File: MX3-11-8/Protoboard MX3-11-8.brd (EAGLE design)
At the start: 74 x 99.4 mm, 719 parts, among them J1 DCJ0202

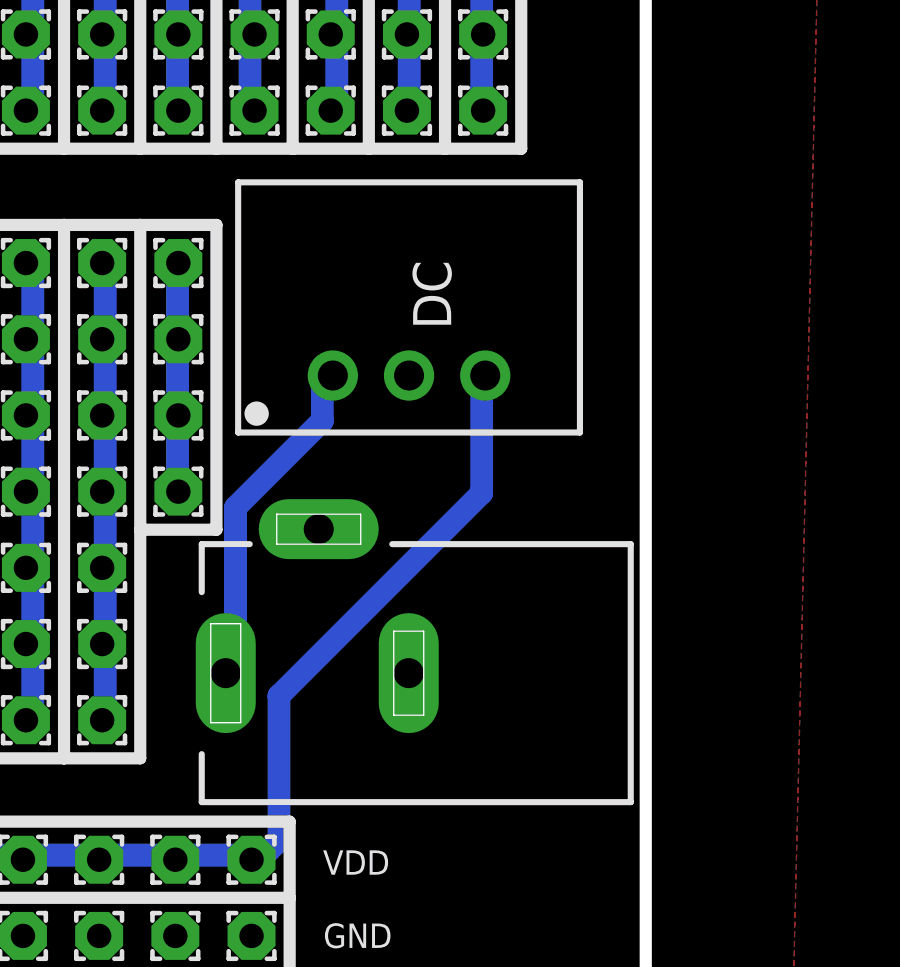
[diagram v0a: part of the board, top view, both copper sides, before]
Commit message: Update Gerb files
Created Gerber files for MX 2-7-6 without ESP
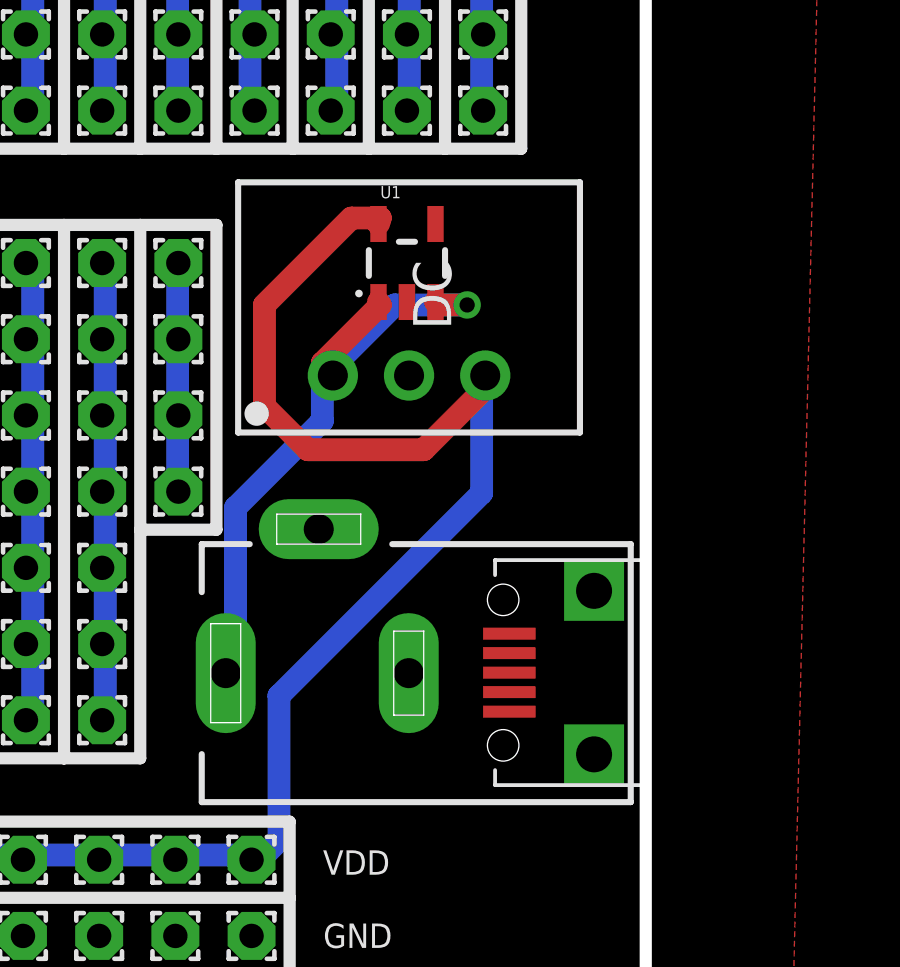
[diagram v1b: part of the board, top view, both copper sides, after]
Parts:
- added JP1: USB-RECEPTABLE, daspilker:FCI-10103594-0001LF
- added U1: 3.3V/150mA, SparkFun-PowerIC:SOT23-5
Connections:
- net GND: now also JP1.5, U1.2
- net VCC: now also JP1.1, U1.1, U1.3
- net VDD: now also U1.5
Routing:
- net VDD: track 226.3 -> 244.6 mm
- net VCC: track 11.6 -> 21.7 mm, vias 0 -> 1
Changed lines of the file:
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@@
 <?xml version="1.0" encoding="utf-8"?>
 <!DOCTYPE eagle SYSTEM "eagle.dtd">
-<eagle version="7.6.0">
+<eagle version="7.7.0">
 <drawing>
 <settings>
@@
 <setting verticaltext="up"/>
 </settings>
-<grid distance="1.27" unitdist="mm" unit="mm" style="dots" multiple="1" display="yes" altdistance="0.1" altunitdist="mm" altunit="mm"/>
+<grid distance="1.27" unitdist="mm" unit="mil" style="dots" multiple="1" display="yes" altdistance="12.5" altunitdist="mil" altunit="mil"/>
 <layers>
 <layer number="1" name="Top" color="4" fill="1" visible="yes" active="yes"/>
@@
 <autorouter>
 <pass name="Default">
-<param name="RoutingGrid" value="0.25mm"/>
+<param name="RoutingGrid" value="9.84251969mil"/>
 <param name="AutoGrid" value="1"/>
-<param name="Efforts" value="0"/>
+<param name="Efforts" value="1"/>
 <param name="TopRouterVariant" value="1"/>
 <param name="tpViaShape" value="round"/>
@@
 <attribute name="VALUE" x="25.4" y="74.26" size="0.0254" layer="27"/>
 </element>
+<element name="U1" library="SparkFun-PowerIC" package="SOT23-5" value="3.3V/150mA" x="66.04" y="27.94">
+<attribute name="PROD_ID" value="VREG-00822" x="66.04" y="27.94" size="1.778" layer="27" display="off"/>
+</element>
+<element name="JP1" library="daspilker" package="FCI-10103594-0001LF" value="USB-RECEPTABLE" x="73.9775" y="14.2875" smashed="yes" rot="R90"/>
 </elements>
 <signals>
@@
 <contactref element="PAD339" pad="1"/>
 <contactref element="PAD331" pad="1"/>
+<contactref element="JP1" pad="5"/>
+<contactref element="U1" pad="2"/>
 </signal>
 <signal name="VCC">
@@
 <wire x1="63.2206" y1="24.13" x2="63.57" y2="24.19" width="0.762" layer="16"/>
 <wire x1="60.325" y1="14.478" x2="60" y2="14.27" width="0.762" layer="16"/>
+<contactref element="JP1" pad="1"/>
+<contactref element="U1" pad="3"/>
+<contactref element="U1" pad="1"/>
+<wire x1="63.2206" y1="24.6126" x2="65.151" y2="26.543" width="0.762" layer="1"/>
+<wire x1="65.151" y1="26.543" x2="65.09" y2="26.6399" width="0.762" layer="1"/>
+<wire x1="63.2206" y1="24.6126" x2="63.57" y2="24.19" width="0.762" layer="1"/>
+<wire x1="68.0466" y1="26.543" x2="67.0814" y2="26.543" width="0.762" layer="1"/>
+<wire x1="65.6336" y1="26.543" x2="68.0466" y2="26.543" width="0.762" layer="16"/>
+<wire x1="63.7032" y1="24.6126" x2="65.6336" y2="26.543" width="0.762" layer="16"/>
+<wire x1="67.0814" y1="26.543" x2="66.99" y2="26.6399" width="0.762" layer="1"/>
+<wire x1="63.7032" y1="24.6126" x2="63.57" y2="24.19" width="0.762" layer="16"/>
+<via x="68.0466" y="26.543" extent="1-16" drill="0.508"/>
+<wire x1="60.325" y1="14.478" x2="69.4525" y2="12.9875" width="0" layer="19" extent="1-16"/>
 </signal>
 <signal name="N$1">
@@
 <wire x1="4.826" y1="91.2114" x2="5.08" y2="91.44" width="0.762" layer="16"/>
 <wire x1="4.826" y1="8.2042" x2="4.98" y2="8.05" width="0.762" layer="16"/>
+<contactref element="U1" pad="5"/>
+<wire x1="64.1858" y1="29.4386" x2="65.151" y2="29.4386" width="0.762" layer="1"/>
+<wire x1="61.2902" y1="26.543" x2="64.1858" y2="29.4386" width="0.762" layer="1"/>
+<wire x1="61.2902" y1="23.1648" x2="61.2902" y2="26.543" width="0.762" layer="1"/>
+<wire x1="62.738" y1="21.717" x2="61.2902" y2="23.1648" width="0.762" layer="1"/>
+<wire x1="66.5988" y1="21.717" x2="62.738" y2="21.717" width="0.762" layer="1"/>
+<wire x1="69.0118" y1="24.13" x2="66.5988" y2="21.717" width="0.762" layer="1"/>
+<wire x1="65.151" y1="29.4386" x2="65.09" y2="29.2401" width="0.762" layer="1"/>
+<wire x1="69.0118" y1="24.13" x2="68.65" y2="24.19" width="0.762" layer="1"/>
 </signal>
 <signal name="N$3">

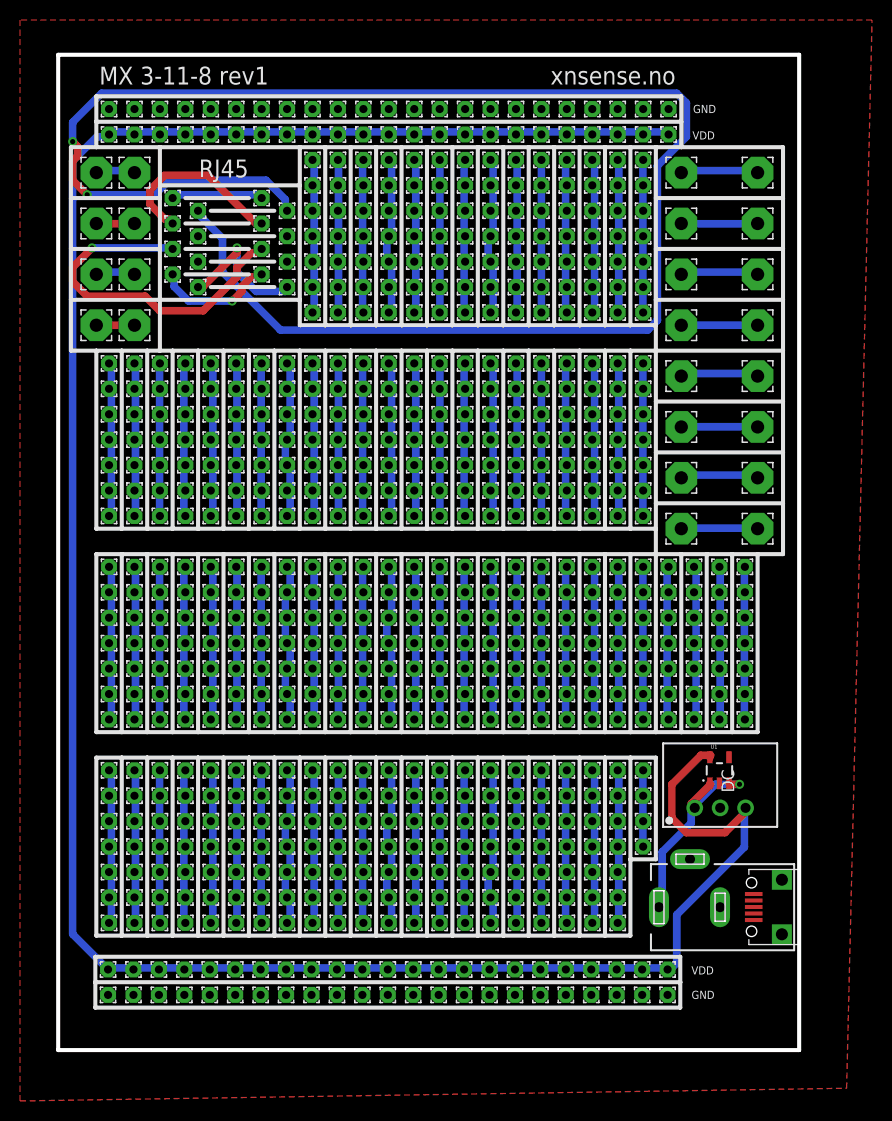
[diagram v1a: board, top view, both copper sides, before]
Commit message: Update to rev2
Updated to Pin headers instead of single wire pads
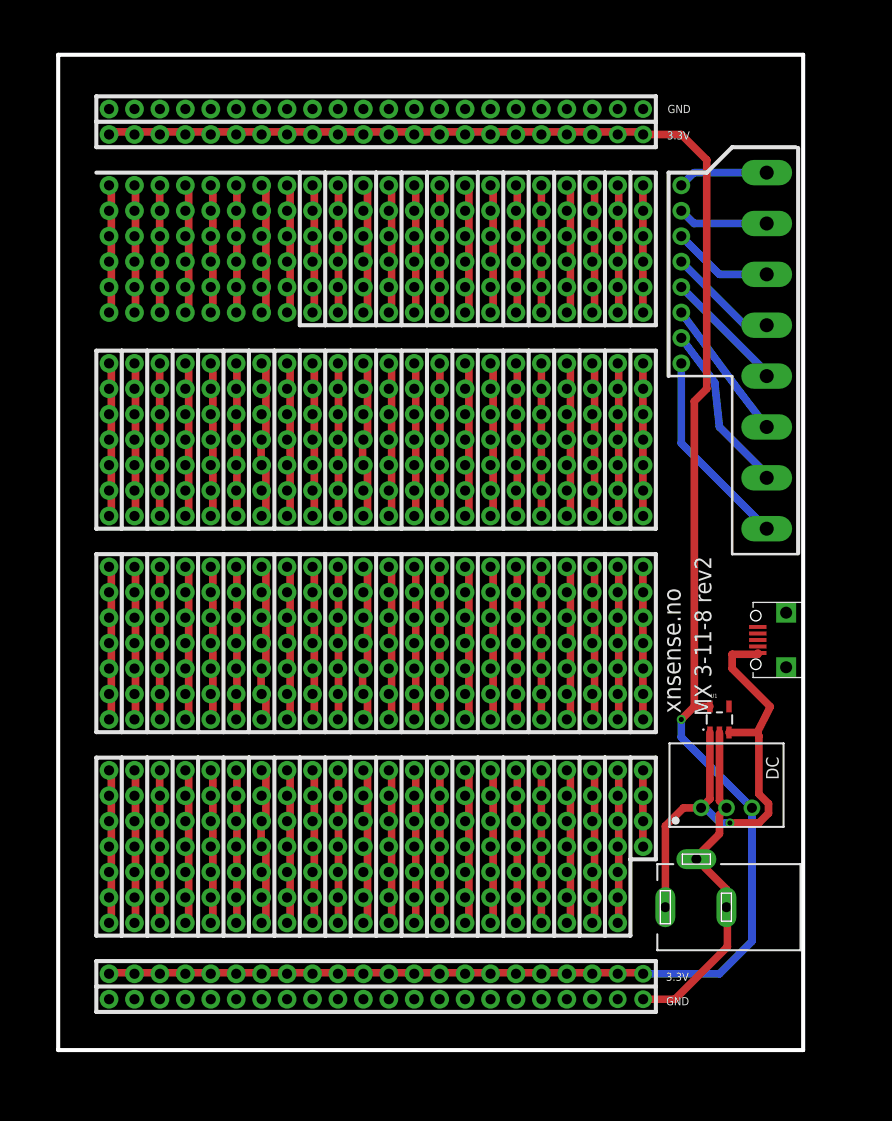
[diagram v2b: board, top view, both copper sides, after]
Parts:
- removed 1, 2, 3, 4, 5, 6, 7, 8, PAD1, PAD10, PAD100, PAD101, PAD102, PAD103, PAD104, PAD105, PAD106, PAD107, PAD108, PAD109, PAD11, PAD110, PAD111, PAD112, PAD113, PAD114, PAD115, PAD116, PAD117, PAD118, PAD119, PAD12, PAD120, PAD121, PAD122, PAD123, PAD124, PAD125, PAD126, PAD127, PAD128, PAD129, PAD13, PAD130, PAD131, PAD132, PAD133, PAD134, PAD135, PAD136, PAD137, PAD138, PAD139, PAD14, PAD140, PAD141, PAD142, PAD143, PAD144, PAD145, PAD146, PAD147, PAD148, PAD149, PAD15, PAD150, PAD151, PAD152, PAD153, PAD154, PAD155, PAD156, PAD157, PAD158, PAD159, PAD16, PAD160, PAD161, PAD162, PAD163, PAD164, PAD165, PAD166, PAD167, PAD168, PAD169, PAD17, PAD170, PAD171, PAD172, PAD173, PAD174, PAD175, PAD176, PAD177, PAD178, PAD179, PAD18, PAD180, PAD181, PAD182, PAD183, PAD184, PAD185, PAD186, PAD187, PAD188, PAD189, PAD19, PAD190, PAD191, PAD192, PAD193, PAD194, PAD195, PAD196, PAD197, PAD198, PAD199, PAD2, PAD20, PAD200, PAD201, PAD202, PAD203, PAD204, PAD205, PAD206, PAD207, PAD208, PAD209, PAD21, PAD210, PAD211, PAD212, PAD213, PAD214, PAD215, PAD216, PAD217, PAD218, PAD219, PAD22, PAD220, PAD221, PAD222, PAD223, PAD224, PAD225, PAD226, PAD227, PAD228, PAD229, PAD23, PAD230, PAD231, PAD232, PAD233, PAD234, PAD235, PAD236, PAD237, PAD238, PAD239, PAD24, PAD240, PAD249, PAD25, PAD250, PAD251, PAD252, PAD253, PAD254, PAD255, PAD26, PAD260, PAD261, PAD262, PAD263, PAD264, PAD265, PAD266, PAD269, PAD27, PAD270, PAD271, PAD272, PAD273, PAD274, PAD275, PAD276, PAD277, PAD278, PAD279, PAD28, PAD280, PAD281, PAD282, PAD283, PAD284, PAD285, PAD286, PAD287, PAD288, PAD289, PAD29, PAD290, PAD291, PAD292, PAD293, PAD294, PAD295, PAD296, PAD297, PAD298, PAD299, PAD3, PAD30, PAD300, PAD301, PAD302, PAD303, PAD304, PAD305, PAD306, PAD307, PAD308, PAD309, PAD31, PAD310, PAD311, PAD312, PAD313, PAD314, PAD315, PAD316, PAD317, PAD318, PAD319, PAD32, PAD320, PAD321, PAD322, PAD323, PAD324, PAD325, PAD326, PAD327, PAD328, PAD329, PAD33, PAD330, PAD331, PAD332, PAD333, PAD334, PAD335, PAD336, PAD337, PAD338, PAD339, PAD34, PAD340, PAD341, PAD342, PAD343, PAD344, PAD345, PAD346, PAD347, PAD348, PAD349, PAD35, PAD350, PAD351, PAD352, PAD353, PAD354, PAD355, PAD356, PAD357, PAD358, PAD359, PAD36, PAD360, PAD361, PAD362, PAD363, PAD364, PAD365, PAD366, PAD367, PAD368, PAD369, PAD37, PAD370, PAD371, PAD372, PAD373, PAD374, PAD375, PAD376, PAD377, PAD378, PAD379, PAD38, PAD380, PAD381, PAD382, PAD383, PAD384, PAD385, PAD386, PAD387, PAD388, PAD389, PAD39, PAD390, PAD391, PAD392, PAD393, PAD394, PAD395, PAD4, PAD40, PAD41, PAD414, PAD415, PAD416, PAD42, PAD420, PAD421, PAD422, PAD423, PAD424, PAD425, PAD426, PAD427, PAD428, PAD429, PAD43, PAD430, PAD431, PAD432, PAD433, PAD434, PAD435, PAD436, PAD437, PAD438, PAD439, PAD44, PAD440, PAD441, PAD442, PAD443, PAD444, PAD445, PAD446, PAD447, PAD448, PAD449, PAD45, PAD450, PAD451, PAD452, PAD453, PAD454, PAD455, PAD456, PAD457, PAD458, PAD459, PAD46, PAD460, PAD461, PAD462, PAD463, PAD464, PAD465, PAD466, PAD467, PAD468, PAD469, PAD47, PAD470, PAD471, PAD472, PAD473, PAD474, PAD475, PAD476, PAD477, PAD478, PAD479, PAD48, PAD480, PAD481, PAD482, PAD483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: (no value), wirepad:1,6/0,8
- removed PAD241, PAD242, PAD243, PAD244, PAD245, PAD246, PAD247, PAD248, PAD734, PAD735, PAD736, PAD737, PAD738, PAD739, PAD740, PAD741, PAD750, PAD751, PAD752, PAD753, PAD754, PAD755, PAD756, PAD757: (no value), wirepad:3,17/1,3
- added J10, J11, J12, J13, J14, J15, J16, J17, J18, J19, J2, J20, J21, J22, J23, J3, J4, J5, J6, J7, J8, J9: (no value), SparkFun-Connectors:1X06_NO_SILK
- added J24, J25, J26, J27, J28, J29, J30, J31, J32, J33, J34, J35, J36, J37, J38, J39, J40, J41, J42, J43, J44, J45, J46, J47, J48, J49, J50, J51, J52, J53, J54, J55, J56, J57, J58, J59, J60, J61, J62, J63, J64, J65, J66, J67, J68, J69, J70, J71, J72, J73, J74, J75, J76, J77, J78, J79, J80, J81, J82, J83, J84, J85, J86, J87, J88: (no value), SparkFun-Connectors:1X07_NO_SILK
- added J89: (no value), SparkFun-Connectors:1X04_NO_SILK_ALL_ROUND
- added J90, J91, J92, J93: (no value), SparkFun-Connectors:1X20_NO_SILK_KIT
- added JP10, JP11, JP12, JP13, JP14, JP15, JP16, JP17, JP18, JP19, JP20, JP21, JP22, JP23, JP24, JP25: (no value), adafruit:1X01-CLEANBIG
- added JP2, JP3, JP4, JP5, JP6, JP7, JP8, JP9: (no value), adafruit:1X1-BIGPOGO
- moved JP1 26.7 mm to (74.4, 41.0)
- moved U1 5.08 mm to (66.0, 33.0)
- moved DC 0.64 mm to (66.7, 24.2)
- moved J1 0.63 mm to (63.7, 14.3)
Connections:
- removed net N$100: PAD699.1, PAD700.1, PAD701.1, PAD702.1, PAD703.1, PAD704.1, PAD705.1
- removed net N$101: PAD706.1, PAD707.1, PAD708.1, PAD709.1, PAD710.1, PAD711.1, PAD712.1
- removed net N$102: 1.1, RJ-1-1.1
- removed net N$103: 2.1, RJ-2-1.1
- removed net N$104: 3.1, RJ-3.1
- removed net N$105: 4.1, RJ-4-1.1
- removed net N$106: 5.1, RJ-5-1.1
- removed net N$107: 6.1, RJ-6-1.1
- removed net N$108: 7.1, RJ-7-1.1
- removed net N$109: 8.1, RJ-8-1.1
- removed net N$110: PAD713.1, PAD714.1, PAD715.1, PAD716.1, PAD717.1, PAD718.1, PAD719.1
- removed net N$111: PAD720.1, PAD721.1, PAD722.1, PAD723.1, PAD724.1, PAD725.1, PAD726.1
- removed net N$112: PAD727.1, PAD728.1, PAD729.1, PAD730.1, PAD731.1, PAD732.1, PAD733.1
- removed net N$113: PAD734.1, PAD757.1
- removed net N$114: PAD735.1, PAD756.1
- removed net N$115: PAD736.1, PAD755.1
- removed net N$116: PAD737.1, PAD754.1
- removed net N$117: PAD738.1, PAD753.1
- removed net N$118: PAD739.1, PAD752.1
- removed net N$119: PAD740.1, PAD751.1
- removed net N$120: PAD741.1, PAD750.1
- removed net N$97: PAD678.1, PAD679.1, PAD680.1, PAD681.1, PAD682.1, PAD683.1, PAD684.1
- removed net N$98: PAD685.1, PAD686.1, PAD687.1, PAD688.1, PAD689.1, PAD690.1, PAD691.1
- removed net N$99: PAD692.1, PAD693.1, PAD694.1, PAD695.1, PAD696.1, PAD697.1, PAD698.1
- new net N$47: J48.1, J48.2, J48.3, J48.4, J48.5, J48.6, J48.7
- new net N$48: J49.1, J49.2, J49.3, J49.4, J49.5, J49.6, J49.7
- new net N$52: J53.1, J53.2, J53.3, J53.4, J53.5, J53.6, J53.7
- new net N$53: J54.1, J54.2, J54.3, J54.4, J54.5, J54.6, J54.7
- new net N$54: J55.1, J55.2, J55.3, J55.4, J55.5, J55.6, J55.7
- new net N$55: J56.1, J56.2, J56.3, J56.4, J56.5, J56.6, J56.7
- new net N$56: J57.1, J57.2, J57.3, J57.4, J57.5, J57.6, J57.7
- new net N$57: J58.1, J58.2, J58.3, J58.4, J58.5, J58.6, J58.7
- new net N$58: J59.1, J59.2, J59.3, J59.4, J59.5, J59.6, J59.7
- new net N$85: J86.1, J86.2, J86.3, J86.4, J86.5, J86.6, J86.7
- new net N$86: J87.1, J87.2, J87.3, J87.4, J87.5, J87.6, J87.7
- new net N$87: J88.1, J88.2, J88.3, J88.4, J88.5, J88.6, J88.7
- new net N$88: J89.1, J89.2, J89.3, J89.4
- new net N$89: JP10.1, JP2.P$1
- new net N$90: JP11.1, JP3.P$1
- new net N$91: JP12.1, JP4.P$1
- net GND: now also J91.1, J91.10, J91.11, J91.12, J91.13, J91.14, J91.15, J91.16, J91.17, J91.18, J91.19, J91.2, J91.20, J91.3, J91.4, J91.5, J91.6, J91.7, J91.8, J91.9, J92.1, J92.10, J92.11, J92.12, J92.13, J92.14, J92.15, J92.16, J92.17, J92.18, J92.19, J92.2, J92.20, J92.3, J92.4, J92.5, J92.6, J92.7, J92.8, J92.9, JP20.1, JP21.1, JP23.1, JP24.1; no longer PAD17.1, PAD22.1, PAD23.1, PAD24.1, PAD25.1, PAD26.1, PAD27.1, PAD276.1, PAD277.1, PAD28.1, PAD285.1, PAD286.1, PAD29.1, PAD30.1, PAD31.1, PAD32.1, PAD326.1, PAD327.1, PAD328.1, PAD329.1, PAD33.1, PAD330.1, PAD331.1, PAD339.1, PAD36.1, PAD38.1, PAD4.1, PAD421.1, PAD422.1, PAD423.1, PAD424.1, PAD425.1, PAD426.1, PAD427.1, PAD428.1, PAD429.1, PAD430.1, PAD431.1, PAD432.1, PAD433.1, PAD434.1, PAD435.1, PAD436.1, PAD439.1, PAD440.1, PAD441.1
- net N$1: now also J2.1, J2.2, J2.3, J2.4, J2.5, J2.6; no longer PAD391.1, PAD392.1, PAD393.1, PAD394.1, PAD42.1, PAD43.1, PAD44.1
- net N$10: now also J11.1, J11.2, J11.3, J11.4, J11.5, J11.6; no longer PAD106.1, PAD107.1, PAD108.1, PAD109.1, PAD110.1, PAD111.1, PAD112.1
- net N$11: now also J12.1, J12.2, J12.3, J12.4, J12.5, J12.6; no longer PAD115.1, PAD116.1, PAD117.1, PAD118.1, PAD119.1, PAD120.1, PAD121.1
- net N$12: now also J13.1, J13.2, J13.3, J13.4, J13.5, J13.6; no longer PAD124.1, PAD125.1, PAD126.1, PAD127.1, PAD128.1, PAD129.1, PAD130.1
- net N$13: now also J14.1, J14.2, J14.3, J14.4, J14.5, J14.6; no longer PAD133.1, PAD134.1, PAD135.1, PAD136.1, PAD137.1, PAD138.1, PAD139.1
- net N$14: now also J15.1, J15.2, J15.3, J15.4, J15.5, J15.6; no longer PAD142.1, PAD143.1, PAD144.1, PAD145.1, PAD146.1, PAD147.1, PAD148.1
- net N$15: now also J16.1, J16.2, J16.3, J16.4, J16.5, J16.6; no longer PAD151.1, PAD152.1, PAD153.1, PAD154.1, PAD155.1, PAD156.1, PAD157.1
- net N$16: now also J17.1, J17.2, J17.3, J17.4, J17.5, J17.6; no longer PAD160.1, PAD161.1, PAD162.1, PAD163.1, PAD164.1, PAD165.1, PAD166.1
- net N$17: now also J18.1, J18.2, J18.3, J18.4, J18.5, J18.6; no longer PAD169.1, PAD170.1, PAD171.1, PAD172.1, PAD173.1, PAD174.1, PAD175.1
- net N$18: now also J19.1, J19.2, J19.3, J19.4, J19.5, J19.6; no longer PAD178.1, PAD179.1, PAD180.1, PAD181.1, PAD182.1, PAD183.1, PAD184.1
- net N$19: now also J20.1, J20.2, J20.3, J20.4, J20.5, J20.6; no longer PAD187.1, PAD188.1, PAD189.1, PAD190.1, PAD191.1, PAD192.1, PAD193.1
- net N$2: now also J3.1, J3.2, J3.3, J3.4, J3.5, J3.6; no longer PAD241.1, PAD248.1
- net N$20: now also J21.1, J21.2, J21.3, J21.4, J21.5, J21.6; no longer PAD196.1, PAD197.1, PAD198.1, PAD199.1, PAD200.1, PAD201.1, PAD202.1
- net N$21: now also J22.1, J22.2, J22.3, J22.4, J22.5, J22.6; no longer PAD205.1, PAD206.1, PAD207.1, PAD208.1, PAD209.1, PAD210.1, PAD211.1
- net N$22: now also J23.1, J23.2, J23.3, J23.4, J23.5, J23.6; no longer PAD214.1, PAD215.1, PAD216.1, PAD217.1, PAD218.1, PAD219.1, PAD220.1
- net N$23: now also J24.1, J24.2, J24.3, J24.4, J24.5, J24.6, J24.7; no longer PAD66.1, PAD67.1, PAD68.1, PAD69.1, PAD70.1, PAD71.1, PAD72.1
- net N$24: now also J25.1, J25.2, J25.3, J25.4, J25.5, J25.6, J25.7; no longer PAD73.1, PAD74.1, PAD75.1, PAD76.1, PAD77.1, PAD78.1, PAD86.1
- net N$25: now also J26.1, J26.2, J26.3, J26.4, J26.5, J26.6, J26.7; no longer PAD104.1, PAD105.1, PAD113.1, PAD114.1, PAD87.1, PAD95.1, PAD96.1
- net N$26: now also J27.1, J27.2, J27.3, J27.4, J27.5, J27.6, J27.7; no longer PAD122.1, PAD123.1, PAD131.1, PAD132.1
- net N$27: now also J28.1, J28.2, J28.3, J28.4, J28.5, J28.6, J28.7; no longer PAD260.1, PAD261.1, PAD262.1, PAD263.1, PAD264.1, PAD265.1, PAD266.1
- net N$28: now also J29.1, J29.2, J29.3, J29.4, J29.5, J29.6, J29.7; no longer PAD269.1, PAD270.1, PAD271.1, PAD272.1, PAD273.1, PAD274.1, PAD275.1
- net N$29: now also J30.1, J30.2, J30.3, J30.4, J30.5, J30.6, J30.7; no longer PAD278.1, PAD279.1, PAD280.1, PAD281.1, PAD282.1, PAD283.1, PAD284.1
- net N$3: now also J4.1, J4.2, J4.3, J4.4, J4.5, J4.6; no longer PAD1.1, PAD2.1, PAD3.1, PAD34.1, PAD35.1, PAD37.1, PAD40.1
- net N$30: now also J31.1, J31.2, J31.3, J31.4, J31.5, J31.6, J31.7; no longer PAD287.1, PAD288.1, PAD289.1, PAD290.1, PAD291.1, PAD292.1, PAD293.1
- net N$31: now also J32.1, J32.2, J32.3, J32.4, J32.5, J32.6, J32.7; no longer PAD296.1, PAD297.1, PAD298.1, PAD299.1, PAD300.1, PAD301.1, PAD302.1
- net N$32: now also J33.1, J33.2, J33.3, J33.4, J33.5, J33.6, J33.7; no longer PAD305.1, PAD306.1, PAD307.1, PAD308.1, PAD309.1, PAD310.1, PAD311.1
- net N$33: now also J34.1, J34.2, J34.3, J34.4, J34.5, J34.6, J34.7; no longer PAD314.1, PAD315.1, PAD316.1, PAD317.1, PAD318.1, PAD319.1, PAD320.1
- net N$34: now also J35.1, J35.2, J35.3, J35.4, J35.5, J35.6, J35.7; no longer PAD150.1, PAD158.1, PAD159.1, PAD167.1, PAD168.1, PAD176.1, PAD177.1
- net N$35: now also J36.1, J36.2, J36.3, J36.4, J36.5, J36.6, J36.7; no longer PAD332.1, PAD333.1, PAD334.1, PAD335.1, PAD336.1, PAD337.1, PAD338.1
- net N$36: now also J37.1, J37.2, J37.3, J37.4, J37.5, J37.6, J37.7; no longer PAD341.1, PAD342.1, PAD343.1, PAD344.1, PAD345.1, PAD346.1, PAD347.1
- net N$37: now also J38.1, J38.2, J38.3, J38.4, J38.5, J38.6, J38.7; no longer PAD350.1, PAD351.1, PAD352.1, PAD353.1, PAD354.1, PAD355.1, PAD356.1
- net N$38: now also J39.1, J39.2, J39.3, J39.4, J39.5, J39.6, J39.7; no longer PAD359.1, PAD360.1, PAD361.1, PAD362.1, PAD363.1, PAD364.1, PAD365.1
- net N$39: now also J40.1, J40.2, J40.3, J40.4, J40.5, J40.6, J40.7; no longer PAD368.1, PAD369.1, PAD370.1, PAD371.1, PAD372.1, PAD373.1, PAD374.1
- net N$4: now also J5.1, J5.2, J5.3, J5.4, J5.5, J5.6; no longer PAD45.1, PAD46.1, PAD47.1, PAD48.1, PAD49.1, PAD50.1, PAD51.1
- net N$40: now also J41.1, J41.2, J41.3, J41.4, J41.5, J41.6, J41.7; no longer PAD377.1, PAD378.1, PAD379.1, PAD380.1, PAD381.1, PAD382.1, PAD383.1
- net N$41: now also J42.1, J42.2, J42.3, J42.4, J42.5, J42.6, J42.7; no longer PAD385.1, PAD386.1, PAD387.1, PAD388.1, PAD389.1, PAD39.1, PAD41.1
- net N$42: now also J43.1, J43.2, J43.3, J43.4, J43.5, J43.6, J43.7; no longer PAD242.1, PAD247.1
- net N$43: now also J44.1, J44.2, J44.3, J44.4, J44.5, J44.6, J44.7; no longer PAD243.1, PAD246.1
- net N$44: now also J45.1, J45.2, J45.3, J45.4, J45.5, J45.6, J45.7; no longer PAD244.1, PAD245.1
- net N$45: now also J46.1, J46.2, J46.3, J46.4, J46.5, J46.6, J46.7; no longer PAD185.1, PAD186.1, PAD194.1, PAD195.1, PAD203.1, PAD204.1, PAD212.1
- net N$46: now also J47.1, J47.2, J47.3, J47.4, J47.5, J47.6, J47.7; no longer PAD249.1, PAD250.1, PAD251.1, PAD252.1, PAD253.1, PAD254.1, PAD255.1
- net N$49: now also J50.1, J50.2, J50.3, J50.4, J50.5, J50.6, J50.7; no longer PAD213.1, PAD221.1, PAD222.1, PAD223.1, PAD224.1, PAD225.1, PAD226.1
- net N$5: now also J6.1, J6.2, J6.3, J6.4, J6.5, J6.6; no longer PAD52.1, PAD53.1, PAD54.1, PAD55.1, PAD56.1, PAD57.1, PAD58.1
- net N$50: now also J51.1, J51.2, J51.3, J51.4, J51.5, J51.6, J51.7; no longer PAD227.1, PAD228.1, PAD229.1, PAD230.1, PAD231.1, PAD232.1, PAD233.1
- net N$51: now also J52.1, J52.2, J52.3, J52.4, J52.5, J52.6, J52.7; no longer PAD234.1, PAD235.1, PAD236.1, PAD237.1, PAD238.1, PAD239.1, PAD240.1
- net N$59: now also J60.1, J60.2, J60.3, J60.4, J60.5, J60.6, J60.7; no longer PAD340.1, PAD348.1, PAD349.1, PAD357.1, PAD358.1, PAD366.1, PAD367.1
- net N$6: now also J7.1, J7.2, J7.3, J7.4, J7.5, J7.6; no longer PAD59.1, PAD60.1, PAD61.1, PAD62.1, PAD63.1, PAD64.1, PAD65.1
- net N$60: now also J61.1, J61.2, J61.3, J61.4, J61.5, J61.6, J61.7; no longer PAD375.1, PAD376.1, PAD384.1, PAD390.1, PAD395.1, PAD414.1, PAD415.1
- net N$61: now also J62.1, J62.2, J62.3, J62.4, J62.5, J62.6, J62.7; no longer PAD416.1, PAD420.1, PAD437.1, PAD438.1, PAD457.1, PAD458.1, PAD463.1
- net N$62: now also J63.1, J63.2, J63.3, J63.4, J63.5, J63.6, J63.7; no longer PAD464.1, PAD465.1, PAD466.1, PAD467.1, PAD468.1, PAD469.1, PAD470.1
- net N$63: now also J64.1, J64.2, J64.3, J64.4, J64.5, J64.6, J64.7; no longer PAD140.1, PAD141.1, PAD149.1, PAD471.1, PAD472.1, PAD473.1, PAD474.1
- net N$64: now also J65.1, J65.2, J65.3, J65.4, J65.5, J65.6, J65.7; no longer PAD475.1, PAD476.1, PAD477.1, PAD478.1, PAD479.1, PAD480.1, PAD481.1
- net N$65: now also J66.1, J66.2, J66.3, J66.4, J66.5, J66.6, J66.7; no longer PAD482.1, PAD483.1, PAD484.1, PAD485.1, PAD486.1, PAD487.1, PAD488.1
- net N$66: now also J67.1, J67.2, J67.3, J67.4, J67.5, J67.6, J67.7; no longer PAD489.1, PAD490.1, PAD491.1, PAD492.1, PAD493.1, PAD494.1, PAD495.1
- net N$67: now also J68.1, J68.2, J68.3, J68.4, J68.5, J68.6, J68.7; no longer PAD496.1, PAD497.1, PAD498.1, PAD499.1, PAD500.1, PAD501.1, PAD502.1
- net N$68: now also J69.1, J69.2, J69.3, J69.4, J69.5, J69.6, J69.7; no longer PAD503.1, PAD504.1, PAD505.1, PAD506.1, PAD507.1, PAD508.1, PAD509.1
- net N$69: now also J70.1, J70.2, J70.3, J70.4, J70.5, J70.6, J70.7; no longer PAD510.1, PAD511.1, PAD512.1, PAD513.1, PAD514.1, PAD515.1, PAD516.1
- net N$7: now also J8.1, J8.2, J8.3, J8.4, J8.5, J8.6; no longer PAD79.1, PAD80.1, PAD81.1, PAD82.1, PAD83.1, PAD84.1, PAD85.1
- net N$70: now also J71.1, J71.2, J71.3, J71.4, J71.5, J71.6, J71.7; no longer PAD517.1, PAD518.1, PAD519.1, PAD520.1, PAD521.1, PAD522.1, PAD523.1
- net N$71: now also J72.1, J72.2, J72.3, J72.4, J72.5, J72.6, J72.7; no longer PAD524.1, PAD525.1, PAD526.1, PAD527.1, PAD528.1, PAD529.1, PAD530.1
- net N$72: now also J73.1, J73.2, J73.3, J73.4, J73.5, J73.6, J73.7; no longer PAD531.1, PAD532.1, PAD533.1, PAD534.1, PAD535.1, PAD536.1, PAD537.1
- net N$73: now also J74.1, J74.2, J74.3, J74.4, J74.5, J74.6, J74.7; no longer PAD538.1, PAD539.1, PAD540.1, PAD541.1, PAD542.1, PAD543.1, PAD544.1
- net N$74: now also J75.1, J75.2, J75.3, J75.4, J75.5, J75.6, J75.7; no longer PAD545.1, PAD546.1, PAD547.1, PAD548.1, PAD549.1, PAD550.1, PAD551.1
- net N$75: now also J76.1, J76.2, J76.3, J76.4, J76.5, J76.6, J76.7; no longer PAD552.1, PAD553.1, PAD554.1, PAD555.1, PAD556.1, PAD557.1, PAD558.1
- net N$76: now also J77.1, J77.2, J77.3, J77.4, J77.5, J77.6, J77.7; no longer PAD559.1, PAD560.1, PAD561.1, PAD562.1, PAD563.1, PAD564.1, PAD565.1
- net N$77: now also J78.1, J78.2, J78.3, J78.4, J78.5, J78.6, J78.7; no longer PAD566.1, PAD567.1, PAD568.1, PAD569.1, PAD570.1, PAD571.1, PAD572.1
- net N$78: now also J79.1, J79.2, J79.3, J79.4, J79.5, J79.6, J79.7; no longer PAD573.1, PAD574.1, PAD575.1, PAD576.1, PAD577.1, PAD578.1, PAD579.1
- net N$79: now also J80.1, J80.2, J80.3, J80.4, J80.5, J80.6, J80.7; no longer PAD580.1, PAD581.1, PAD582.1, PAD583.1, PAD584.1, PAD585.1, PAD586.1
- net N$8: now also J9.1, J9.2, J9.3, J9.4, J9.5, J9.6; no longer PAD88.1, PAD89.1, PAD90.1, PAD91.1, PAD92.1, PAD93.1, PAD94.1
- net N$80: now also J81.1, J81.2, J81.3, J81.4, J81.5, J81.6, J81.7; no longer PAD587.1, PAD588.1, PAD589.1, PAD590.1, PAD591.1, PAD592.1, PAD593.1
- net N$81: now also J82.1, J82.2, J82.3, J82.4, J82.5, J82.6, J82.7; no longer PAD594.1, PAD595.1, PAD596.1, PAD597.1, PAD598.1, PAD599.1, PAD600.1
- net N$82: now also J83.1, J83.2, J83.3, J83.4, J83.5, J83.6, J83.7; no longer PAD601.1, PAD602.1, PAD603.1, PAD604.1, PAD605.1, PAD606.1, PAD607.1
- net N$83: now also J84.1, J84.2, J84.3, J84.4, J84.5, J84.6, J84.7; no longer PAD608.1, PAD609.1, PAD610.1, PAD611.1, PAD612.1, PAD613.1, PAD614.1
- net N$84: now also J85.1, J85.2, J85.3, J85.4, J85.5, J85.6, J85.7; no longer PAD615.1, PAD616.1, PAD617.1, PAD618.1, PAD619.1, PAD620.1, PAD621.1
- net N$9: now also J10.1, J10.2, J10.3, J10.4, J10.5, J10.6; no longer PAD100.1, PAD101.1, PAD102.1, PAD103.1, PAD97.1, PAD98.1, PAD99.1
- net N$92: now also JP13.1, JP5.P$1; no longer PAD643.1, PAD644.1, PAD645.1, PAD646.1, PAD647.1, PAD648.1, PAD649.1
- net N$93: now also JP14.1, JP6.P$1; no longer PAD650.1, PAD651.1, PAD652.1, PAD653.1, PAD654.1, PAD655.1, PAD656.1
- net N$94: now also JP15.1, JP7.P$1; no longer PAD657.1, PAD658.1, PAD659.1, PAD660.1, PAD661.1, PAD662.1, PAD663.1
- net N$95: now also JP16.1, JP8.P$1; no longer PAD664.1, PAD665.1, PAD666.1, PAD667.1, PAD668.1, PAD669.1, PAD670.1
- net N$96: now also JP17.1, JP9.P$1; no longer PAD671.1, PAD672.1, PAD673.1, PAD674.1, PAD675.1, PAD676.1, PAD677.1
- net VDD: now also J90.1, J90.10, J90.11, J90.12, J90.13, J90.14, J90.15, J90.16, J90.17, J90.18, J90.19, J90.2, J90.20, J90.3, J90.4, J90.5, J90.6, J90.7, J90.8, J90.9, J93.1, J93.10, J93.11, J93.12, J93.13, J93.14, J93.15, J93.16, J93.17, J93.18, J93.19, J93.2, J93.20, J93.3, J93.4, J93.5, J93.6, J93.7, J93.8, J93.9, JP18.1, JP19.1, JP22.1, JP25.1; no longer PAD10.1, PAD11.1, PAD12.1, PAD13.1, PAD14.1, PAD15.1, PAD16.1, PAD18.1, PAD19.1, PAD20.1, PAD21.1, PAD294.1, PAD295.1, PAD303.1, PAD304.1, PAD312.1, PAD313.1, PAD321.1, PAD322.1, PAD323.1, PAD324.1, PAD325.1, PAD442.1, PAD443.1, PAD444.1, PAD445.1, PAD446.1, PAD447.1, PAD448.1, PAD449.1, PAD450.1, PAD451.1, PAD452.1, PAD453.1, PAD454.1, PAD455.1, PAD456.1, PAD459.1, PAD460.1, PAD461.1, PAD462.1, PAD5.1, PAD6.1, PAD7.1, PAD8.1, PAD9.1
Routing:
- net N$106: track 169.8 -> 0.00 mm, vias 2 -> 0
- net N$104: track 35.6 -> 0.00 mm, vias 1 -> 0
- net GND: track 0.00 -> 34.8 mm
- net VCC: track 21.7 -> 51.8 mm
- net VDD: track 244.6 -> 216.4 mm, vias 0 -> 1
- net N$103: track 18.3 -> 0.00 mm
- net N$55: track 0.00 -> 17.9 mm
- net N$48: track 0.00 -> 17.5 mm
- net N$85: track 0.00 -> 17.5 mm
- net N$52: track 0.00 -> 17.3 mm
- net N$56: track 0.00 -> 17.1 mm
- net N$110: track 17.0 -> 0.00 mm
- net N$98: track 16.8 -> 0.00 mm
- net N$86: track 0.00 -> 16.4 mm
- net N$53: track 0.00 -> 16.2 mm
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- added copper zone on layer 16, net N$97
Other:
- board size 74 x 99.4 mm -> 74.4 x 99.4 mm
- board text added: "3.3V"
- board text added: "MX 3-11-8 rev2"
- board text added: "VCC"
- board text removed: "MX 3-11-8 rev1"
- board text removed: "RJ45"
- board text removed: "VDD"

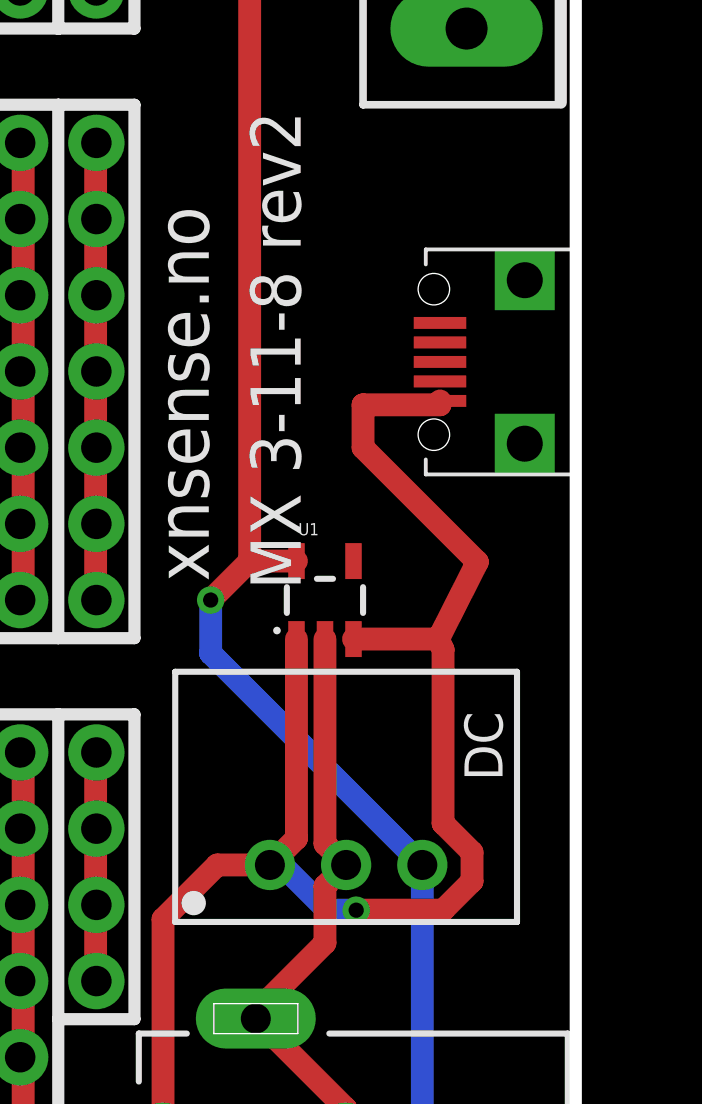
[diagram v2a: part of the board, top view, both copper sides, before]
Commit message: Change usb connector
Change to correct usb connecter and moved esp8266 bit more onto the
board.
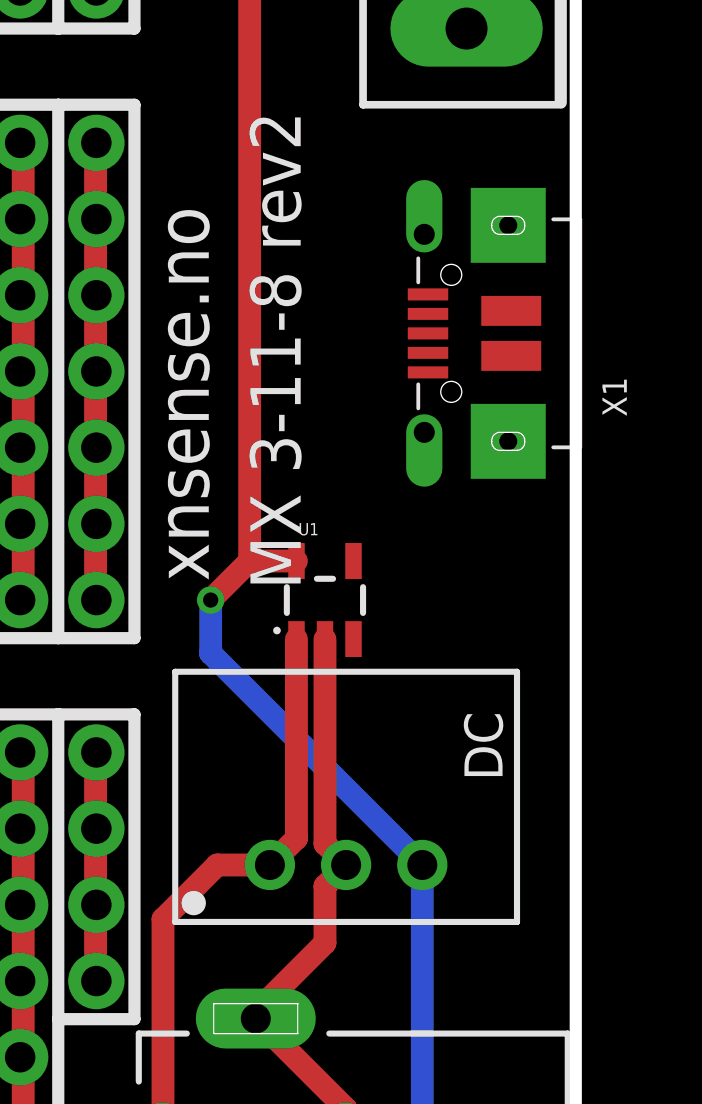
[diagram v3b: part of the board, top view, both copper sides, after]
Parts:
- removed JP1: USB-RECEPTABLE, daspilker:FCI-10103594-0001LF
- added X1: (no value), microbuilder:4UCONN_20329
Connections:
- net GND: now also X1.BASE@1, X1.BASE@2, X1.GND, X1.SPRT@1, X1.SPRT@2, X1.SPRT@3, X1.SPRT@4; no longer JP1.5
- net VCC: now also X1.VBUS; no longer JP1.1
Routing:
- net VCC: track 51.8 -> 20.3 mm, vias 1 -> 0

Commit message: Update esp component and usb
test
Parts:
- moved U1 1.27 mm to (64.8, 33.0)
- moved JP4 0.64 mm to (70.8, 76.8)
- moved JP5 0.64 mm to (70.8, 71.8)
- moved JP6 0.64 mm to (70.8, 66.7)
- moved JP7 0.63 mm to (70.8, 61.6)
- moved JP8 0.63 mm to (70.8, 56.5)
- moved JP9 0.63 mm to (70.8, 51.4)
- moved JP2 0.63 mm to (70.8, 87.0)
- moved JP3 0.63 mm to (70.8, 81.9)
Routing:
- net GND: track 34.8 -> 0.00 mm
- net VCC: track 20.3 -> 41.0 mm
- net VDD: track 216.4 -> 209.2 mm, vias 1 -> 0
- net N$94: track 14.3 -> 15.6 mm
- net N$95: track 17.1 -> 18.0 mm
- net N$96: track 20.0 -> 20.8 mm
- net N$93: track 12.4 -> 13.0 mm
- net N$89: track 9.06 -> 9.62 mm
